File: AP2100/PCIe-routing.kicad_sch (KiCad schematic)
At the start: 38 parts, among them J12 10018783-11200TLF, U15 AP64501SP-13

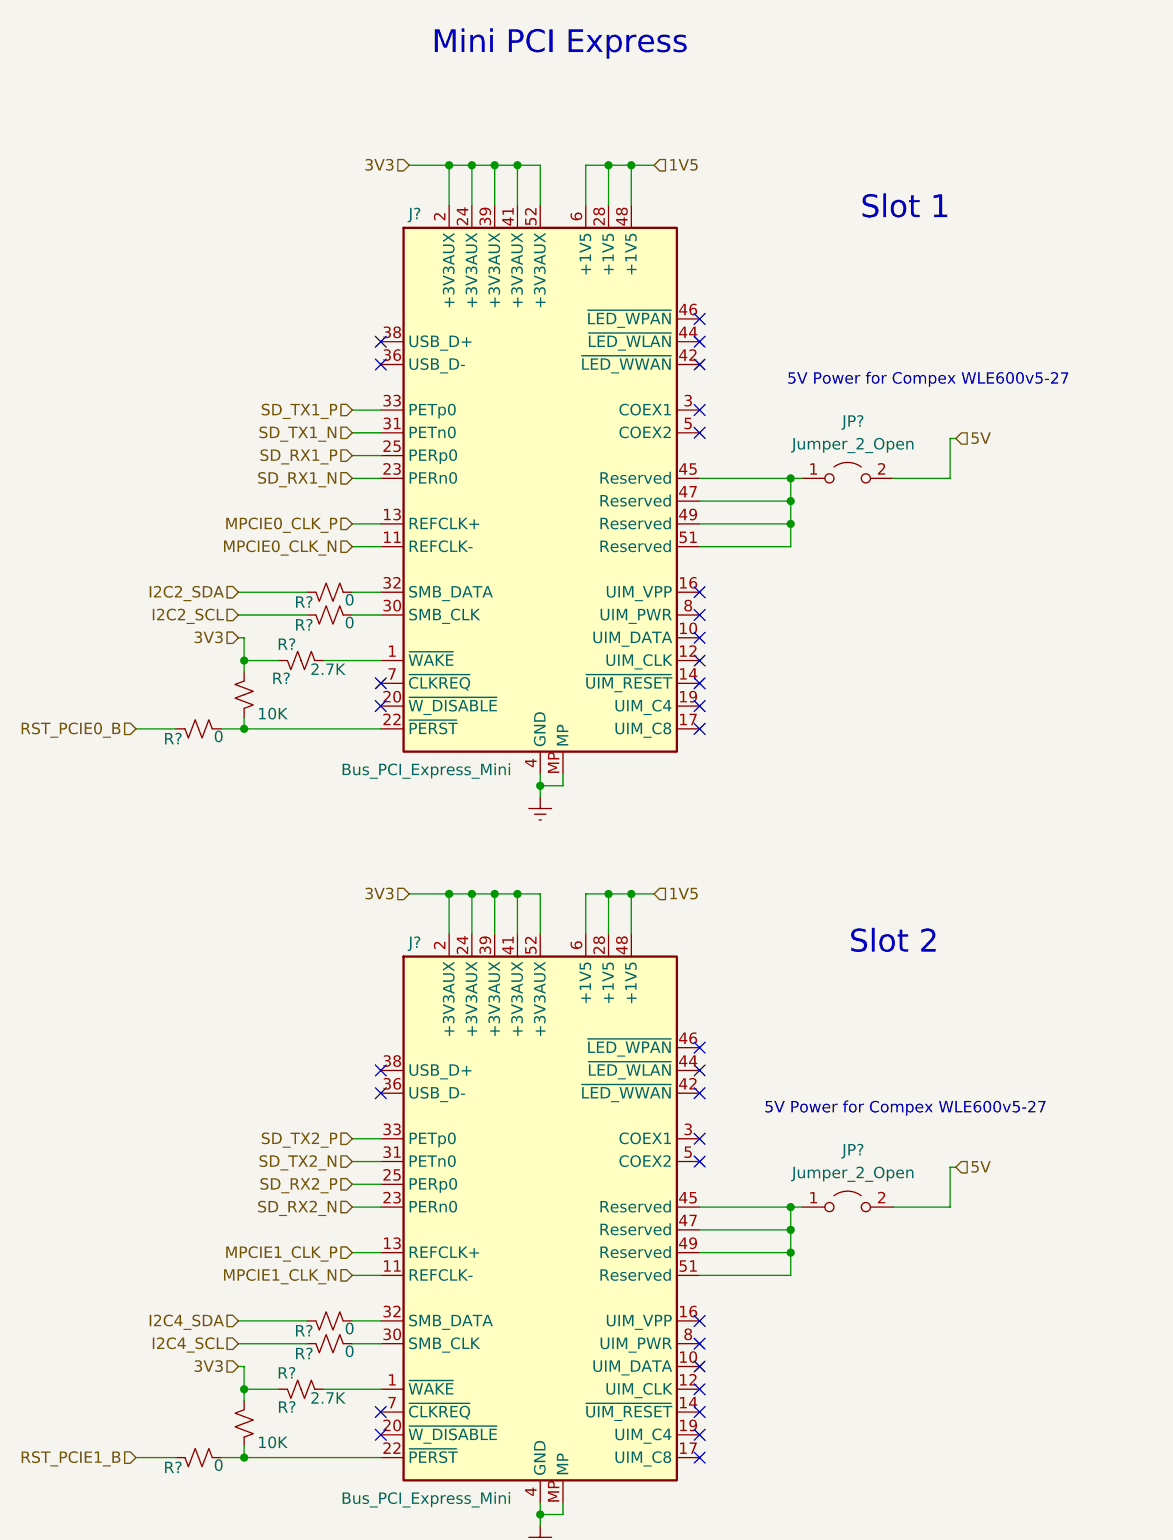
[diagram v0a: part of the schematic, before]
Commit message: Finish PoE section Rename CM4IO library as AP2100
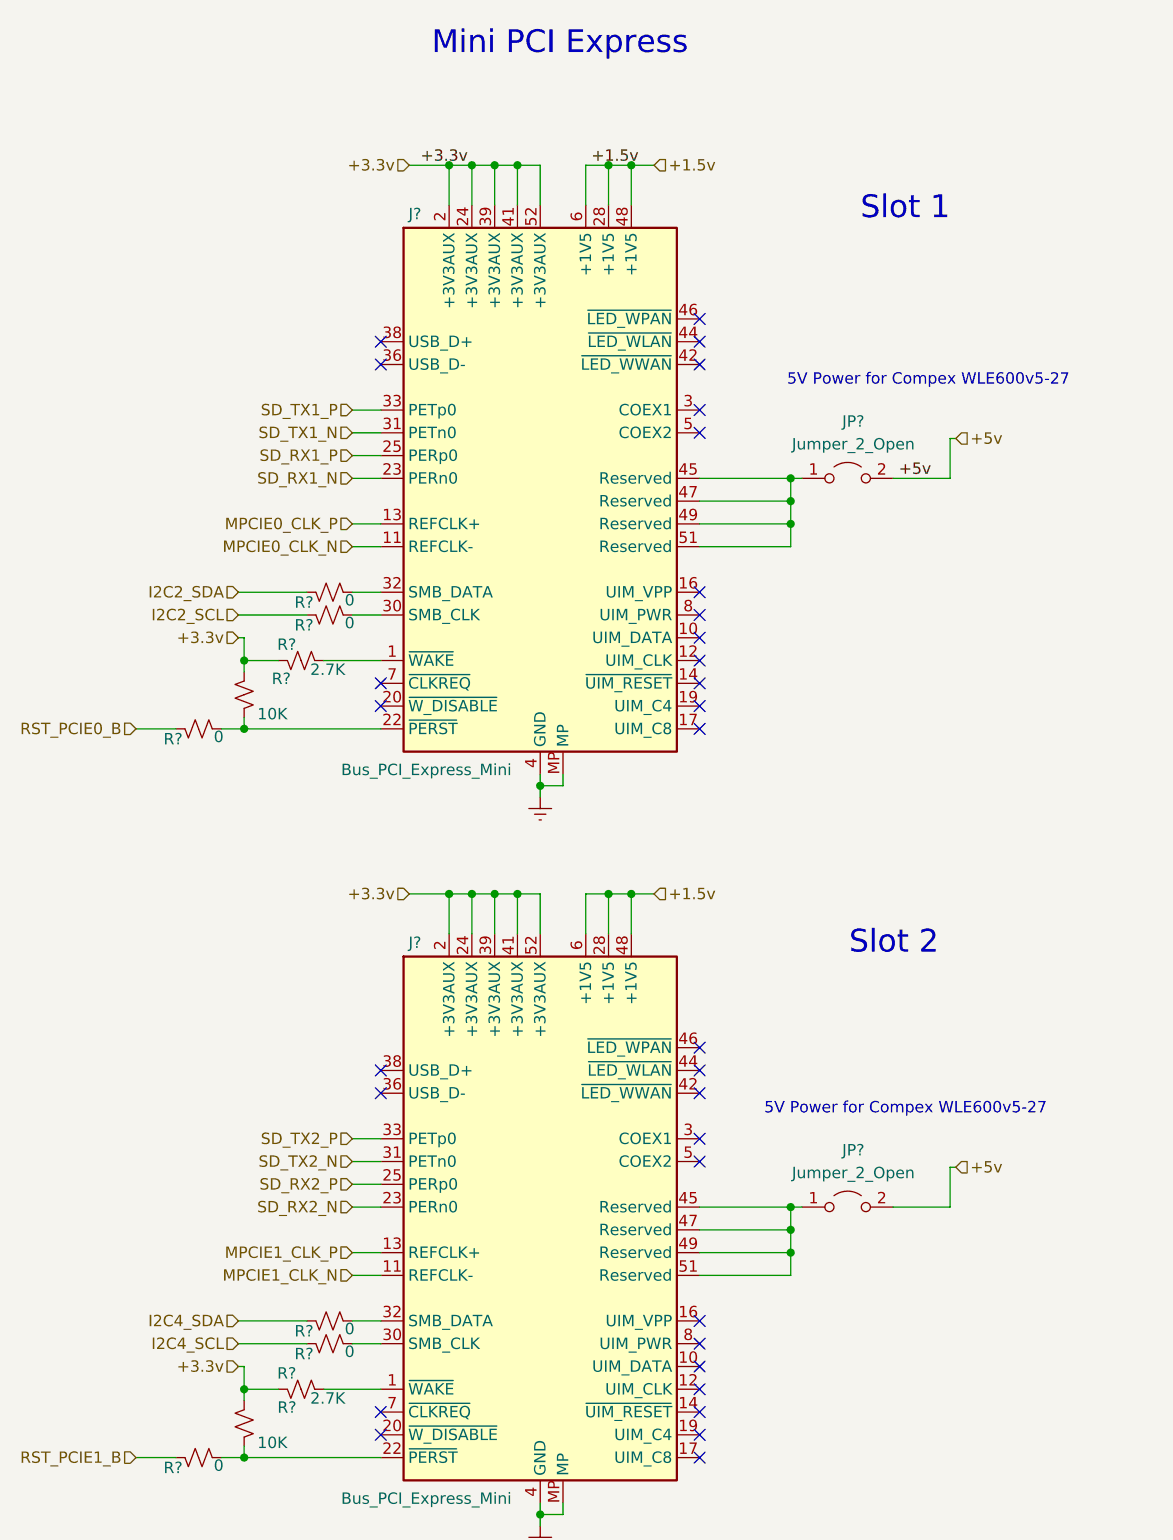
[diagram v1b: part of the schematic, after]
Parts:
- J12: footprint CM4IO:PCIex1-36 -> AP2100:PCIex1-36; symbol CM4IO:PCIe-x1 -> AP2100:PCIe-x1
- U15: symbol CM4IO:AP64351 -> AP2100:AP64351
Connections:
- net 3V3 is gone; now on net +3.3v: J?.2 (+3V3AUX), J?.2 (+3V3AUX), J?.24 (+3V3AUX), J?.24 (+3V3AUX), J?.39 (+3V3AUX), J?.39 (+3V3AUX), J?.41 (+3V3AUX), J?.41 (+3V3AUX), J?.52 (+3V3AUX), J?.52 (+3V3AUX), R?.1, R?.1, R?.2, R?.2
- net 1V5 renamed +1.5v
- net 5V renamed +5v
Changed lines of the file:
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@@
   (junction (at 374.65 102.87) (diameter 1.016) (color 0 0 0 0))
   (junction (at 374.65 105.41) (diameter 1.016) (color 0 0 0 0))
+  (no_connect (at 96.52 139.7))
+  (no_connect (at 60.96 99.06))
+  (no_connect (at 341.63 97.79))
+  (no_connect (at 96.52 182.88))
+  (no_connect (at 60.96 142.24))
+  (no_connect (at 96.52 180.34))
+  (no_connect (at 96.52 175.26))
+  (no_connect (at 96.52 167.64))
+  (no_connect (at 96.52 66.04))
+  (no_connect (at 96.52 86.36))
+  (no_connect (at 96.52 58.42))
+  (no_connect (at 96.52 101.6))
+  (no_connect (at 96.52 91.44))
+  (no_connect (at 60.96 58.42))
   (no_connect (at 60.96 177.8))
-  (no_connect (at 60.96 58.42))
-  (no_connect (at 96.52 167.64))
-  (no_connect (at 96.52 101.6))
+  (no_connect (at 96.52 172.72))
+  (no_connect (at 96.52 96.52))
+  (no_connect (at 60.96 96.52))
+  (no_connect (at 96.52 88.9))
   (no_connect (at 60.96 60.96))
-  (no_connect (at 96.52 66.04))
+  (no_connect (at 96.52 137.16))
+  (no_connect (at 96.52 147.32))
+  (no_connect (at 96.52 142.24))
+  (no_connect (at 341.63 95.25))
+  (no_connect (at 370.84 85.09))
+  (no_connect (at 370.84 100.33))
+  (no_connect (at 96.52 177.8))
+  (no_connect (at 341.63 110.49))
+  (no_connect (at 96.52 60.96))
+  (no_connect (at 96.52 149.86))
+  (no_connect (at 96.52 99.06))
+  (no_connect (at 96.52 68.58))
+  (no_connect (at 341.63 125.73))
+  (no_connect (at 96.52 93.98))
+  (no_connect (at 60.96 139.7))
+  (no_connect (at 96.52 55.88))
   (no_connect (at 60.96 180.34))
-  (no_connect (at 96.52 68.58))
-  (no_connect (at 370.84 85.09))
-  (no_connect (at 96.52 55.88))
-  (no_connect (at 96.52 139.7))
-  (no_connect (at 96.52 91.44))
-  (no_connect (at 60.96 96.52))
-  (no_connect (at 96.52 182.88))
-  (no_connect (at 96.52 149.86))
-  (no_connect (at 96.52 177.8))
-  (no_connect (at 96.52 99.06))
-  (no_connect (at 96.52 172.72))
-  (no_connect (at 96.52 86.36))
-  (no_connect (at 341.63 110.49))
-  (no_connect (at 96.52 175.26))
-  (no_connect (at 96.52 137.16))
-  (no_connect (at 96.52 60.96))
-  (no_connect (at 96.52 58.42))
-  (no_connect (at 60.96 142.24))
   (no_connect (at 96.52 170.18))
-  (no_connect (at 341.63 125.73))
-  (no_connect (at 96.52 88.9))
-  (no_connect (at 370.84 100.33))
-  (no_connect (at 341.63 95.25))
-  (no_connect (at 96.52 147.32))
-  (no_connect (at 96.52 180.34))
-  (no_connect (at 96.52 93.98))
-  (no_connect (at 341.63 97.79))
-  (no_connect (at 96.52 96.52))
-  (no_connect (at 60.96 99.06))
-  (no_connect (at 60.96 139.7))
-  (no_connect (at 96.52 142.24))
   (wire (pts (xy -302.26 59.69) (xy -302.26 63.5))
     (stroke (width 0) (type solid) (color 0 0 0 0))
@@
     (effects (font (size 1.27 1.27)) (justify left bottom))
   )
+  (label "+3.3v" (at 65.405 38.735 0)
+    (effects (font (size 1.27 1.27)) (justify left bottom))
+  )
+  (label "+1.5v" (at 84.455 38.735 0)
+    (effects (font (size 1.27 1.27)) (justify left bottom))
+  )
+  (label "+5v" (at 118.745 73.66 0)
+    (effects (font (size 1.27 1.27)) (justify left bottom))
+  )
   (label "+12v" (at 330.2 85.09 0)
     (effects (font (size 1.27 1.27)) (justify left bottom))
@@
     (effects (font (size 1.27 1.27)) (justify right))
   )
-  (hierarchical_label "3V3" (shape input) (at 45.085 91.44 180)
+  (hierarchical_label "+3.3v" (shape input) (at 45.085 91.44 180)
     (effects (font (size 1.27 1.27)) (justify right))
   )
@@
     (effects (font (size 1.27 1.27)) (justify right))
   )
-  (hierarchical_label "3V3" (shape input) (at 45.085 172.72 180)
+  (hierarchical_label "+3.3v" (shape input) (at 45.085 172.72 180)
     (effects (font (size 1.27 1.27)) (justify right))
   )
@@
     (effects (font (size 1.27 1.27)) (justify right))
   )
-  (hierarchical_label "3V3" (shape input) (at 64.135 38.735 180)
-    (effects (font (size 1.27 1.27)) (justify right))
-  )
-  (hierarchical_label "3V3" (shape input) (at 64.135 120.015 180)
-    (effects (font (size 1.27 1.27)) (justify right))
-  )
-  (hierarchical_label "1V5" (shape input) (at 91.44 38.735 0)
+  (hierarchical_label "+3.3v" (shape input) (at 64.135 38.735 180)
+    (effects (font (size 1.27 1.27)) (justify right))
+  )
+  (hierarchical_label "+3.3v" (shape input) (at 64.135 120.015 180)
+    (effects (font (size 1.27 1.27)) (justify right))
+  )
+  (hierarchical_label "+1.5v" (shape input) (at 91.44 38.735 0)
     (effects (font (size 1.27 1.27)) (justify left))
   )
-  (hierarchical_label "1V5" (shape input) (at 91.44 120.015 0)
+  (hierarchical_label "+1.5v" (shape input) (at 91.44 120.015 0)
     (effects (font (size 1.27 1.27)) (justify left))
   )
-  (hierarchical_label "5V" (shape input) (at 125.095 69.215 0)
+  (hierarchical_label "+5v" (shape input) (at 125.095 69.215 0)
     (effects (font (size 1.27 1.27)) (justify left))
   )
-  (hierarchical_label "5V" (shape input) (at 125.095 150.495 0)
+  (hierarchical_label "+5v" (shape input) (at 125.095 150.495 0)
     (effects (font (size 1.27 1.27)) (justify left))
   )
@@
   (symbol (lib_id "AP2100-rescue:GND-Scott") (at 78.74 109.22 0) (mirror y) (unit 1)
     (in_bom yes) (on_board yes)
-    (property "Reference" "#PWR?" (id 0) (at 78.74 115.57 0)
+    (property "Reference" "#PWR0154" (id 0) (at 78.74 115.57 0)
       (effects (font (size 1.27 1.27)) hide)
     )
@@
   (symbol (lib_id "AP2100-rescue:GND-Scott") (at 78.74 190.5 0) (mirror y) (unit 1)
     (in_bom yes) (on_board yes)
-    (property "Reference" "#PWR?" (id 0) (at 78.74 196.85 0)
+    (property "Reference" "#PWR0153" (id 0) (at 78.74 196.85 0)
       (effects (font (size 1.27 1.27)) hide)
     )
@@
     )
   )
-  (symbol (lib_id "CM4IO:AP64351") (at -208.28 52.07 0) (unit 1)
+  (symbol (lib_id "AP2100:AP64351") (at -208.28 52.07 0) (unit 1)
     (in_bom yes) (on_board yes)
     (property "Reference" "U15" (id 0) (at -207.645 42.8244 0))
@@
     )
   )
-  (symbol (lib_id "CM4IO:PCIe-x1") (at 360.68 118.11 0) (unit 1)
+  (symbol (lib_id "AP2100:PCIe-x1") (at 360.68 118.11 0) (unit 1)
     (in_bom yes) (on_board yes)
     (property "Reference" "J12" (id 0) (at 364.49 81.28 0))
     (property "Value" "10018783-11200TLF" (id 1) (at 356.235 80.6704 0))
-    (property "Footprint" "CM4IO:PCIex1-36" (id 2) (at 360.68 118.11 0)
-      (effects (font (size 1.27 1.27)) hide)
-    )
+    (property "Footprint" "AP2100:PCIex1-36" (id 2) (at 360.68 118.11 0)
+      (effects (font (size 1.27 1.27)) hide)
+    )

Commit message: Finish PCie routing
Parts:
- removed C25, C26, C27, C28, C43, C44: 10u 35v, Capacitor_SMD:C_0805_2012Metric, symbol Device:C
- removed C29, C62: 100n, Capacitor_SMD:C_0402_1005Metric, symbol Device:C
- removed C30, C31, C32, C33: 10u, Capacitor_SMD:C_0805_2012Metric, symbol Device:C
- removed C45: 100uF, Capacitor_Tantalum_SMD:CP_EIA-7343-31_Kemet-D, symbol Device:CP
- removed C63, C65: nf, Capacitor_SMD:C_0402_1005Metric, symbol Device:C
- removed C64: 1.2nF, Capacitor_SMD:C_0402_1005Metric, symbol Device:C
- removed J12: 10018783-11200TLF, AP2100:PCIex1-36, symbol AP2100:PCIe-x1
- removed L3: SRN6045TA-3R3Y, Inductor_SMD:L_Bourns_SRN6045TA, symbol pspice:INDUCTOR
- removed R22: 10R, Resistor_SMD:R_0402_1005Metric, symbol Device:R
- removed R23: 12K 1%, Resistor_SMD:R_0402_1005Metric, symbol Device:R
- removed R24: 47K 1%, Resistor_SMD:R_0402_1005Metric, symbol Device:R
- removed R30: 15K 1%, Resistor_SMD:R_0402_1005Metric, symbol Device:R
- removed R? (x6): 0, Resistor_SMD:R_0402_1005Metric, symbol Device:R_Small_US
- removed R? (x2): 2.7K, Resistor_SMD:R_0402_1005Metric, symbol Device:R_Small_US
- removed R? (x2): 10K, Resistor_SMD:R_0402_1005Metric, symbol Device:R_Small_US
- removed TP1: TestPoint, TestPoint:TestPoint_Pad_2.0x2.0mm, symbol Connector:TestPoint
- removed U15: AP64501SP-13, Package_SO:SOIC-8-1EP_3.9x4.9mm_P1.27mm_EP2.95x4.9mm_Mask2.71x3.4mm_ThermalVias, symbol AP2100:AP64351
- added R? (x11): 4.7K 1%, Resistor_SMD:R_0402_1005Metric, symbol Device:R
- added R? (x6): 49.9 1%, Resistor_SMD:R_0402_1005Metric, symbol Device:R
- added R? (x6): 20 1%, Resistor_SMD:R_0402_1005Metric, symbol Device:R
- added R? (x4): 0 1%, Resistor_SMD:R_0402_1005Metric, symbol Device:R
- added R? (x2): 4.7K, Resistor_SMD:R_0402_1005Metric, symbol Device:R
- added R?: 232 1%, Resistor_SMD:R_0402_1005Metric, symbol Device:R
- added R? (x2): DNS 4.7K 1%, Resistor_SMD:R_0402_1005Metric, symbol Device:R
- added R?: 14.3K 1%, Resistor_SMD:R_0402_1005Metric, symbol Device:R
- added TP?: TestPoint, TestPoint:TestPoint_Pad_2.0x2.0mm, symbol Connector:TestPoint
- added U? (x2): XIO3130IZHC, AP2100:XIO3130IZHC, symbol AP2100:XIO3130IZHC
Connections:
- net MPCIE0_CLK_P is gone; now on net P1_REFCLK_N: J?.13 (REFCLK+)
- net MPCIE1_CLK_N is gone; now on net P1_REFCLK_N: J?.11 (REFCLK-)
- net MPCIE1_CLK_P is gone; now on net P1_REFCLK_N: J?.13 (REFCLK+)
- net +1.5v: now also R?.2, R?.2
- net +3.3v: now also R?.2, R?.2, R?.2, R?.2, R?.2, R?.2, R?.2, R?.2
- net GND: now also R?.1, R?.1, R?.1, R?.1, R?.1, R?.1, R?.1, R?.1, R?.1, R?.1, R?.1, R?.2
- net PCIE_CLK_N: now also U?.L2 (UP_REFCKIN)
- net PCIE_CLK_P: now also U?.L1 (UP_REFCKIP)
- net PCIE_CLK_nREQ: now also R?.1, TP?.1, U?.N2 (*CLKREQ_UP)
- net PCIE_RX_N: now also U?.J2 (UP_PERN)
- net PCIE_RX_P: now also U?.J1 (UP_PERP)
- net PCIE_TX_N: now also U?.G2 (UP_PETN)
- net PCIE_TX_P: now also U?.G1 (UP_PETP)
- net PCIE_nRST: now also R?.1, R?.2, U?.B1 (*UP_PERST)
- net at J?.1 (~WAKE): now also R?.1 (x2)
- net at J?.22 (~PERST): now also R?.1 (x2)
- net MPCIE0_CLK_N renamed P1_REFCLK_N
- net P1_REFCLK_N: now also R?.1, R?.1, R?.1, R?.1, R?.1, R?.1, R?.2, R?.2, R?.2, R?.2, R?.2, R?.2
- net SD_RX1_N renamed P1_RX_N
- net P1_RX_N: now also U?.B6 (DN1_PERN)
- net SD_RX1_P renamed P1_RX_P
- net P1_RX_P: now also U?.A6 (DN1_PERP)
- net SD_RX2_N renamed P2_RX_N
- net P2_RX_N: now also U?.F14 (DN2_PERN)
- net SD_RX2_P renamed P2_RX_P
- net P2_RX_P: now also U?.F13 (DN2_PERP)
- net SD_TX1_N renamed P1_TX_N
- net P1_TX_N: now also U?.B8 (DN1_PETN)
- net SD_TX1_P renamed P1_TX_P
- net P1_TX_P: now also U?.A8 (DN1_PETP)
- net SD_TX2_N renamed P2_TX_N
- net P2_TX_N: now also U?.H14 (DN2_PETN)
- net SD_TX2_P renamed P2_TX_P
- net P2_TX_P: now also U?.H13 (DN2_PETP)
- new net: R?.1, U?.A13 (RSVD), U?.B12 (RSVD)
- new net: R?.2, U?.C4 (RSVD)
- new net: R?.2, U?.P5 (DN3_REFCKOP)
- new net: R?.1, U?.B14 (SCL)
- new net: R?.1, R?.1, U?.C2 (*GRST), U?.C3 (*WAKE)
- new net: R?.1, R?.1
- new net: R?.2, U?.E3 (REFR1)
- new net: R?.1, U?.C10 (DN1_DPSTRP)
- new net: R?.2, U?.A9 (DN1_REFCK_OP)
- new net: R?.2, U?.P1 (RSVD)
- new net: R?.1, U?.N4 (DN3_DPSTRP)
- new net: R?.1, U?.D4 (RSVD)
- new net: R?.2, U?.D2 (REFR0)
- new net: R?.1, U?.L13 (DN2_DPSTRP)
- new net: R?.2, U?.B9 (DN1_REFCK_ON)
- new net: R?.2, U?.J14 (DN2_REFCKON)
- new net: R?.2, U?.K14 (DN2_REFCKOP)
- new net: R?.2, U?.P6 (DN3_REFCKON)
- new net P1_PERST#: R?.2, R?.2, U?.B5 (*DN1_PERST)
- new net P2_PERST#: R?.2, R?.2, U?.A2 (*DN2_PERST)
- new net P3_PERST#: R?.2, U?.A1 (*DN3_PERST)
- new net P3_RX_N: U?.P9 (DN3_PERN)
- new net P3_RX_P: U?.N9 (DN3_PERP)
- new net P3_TX_N: U?.P7 (DN3_PETN)
- new net P3_TX_P: U?.N7 (DN3_PETP)
- no-connect marks 38 -> 56
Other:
- note removed: "3.3v @ 3.3A PSU for PCIe Only ( 12v Input )"
- note removed: "NB PCIe x1 takes a maximum of +12v @0.6A or +3.3v@3A , 10Watts combined"
- note removed: "PCIe x1 connector"
- note removed: "TX and RX have PN swaps to improve routing"
